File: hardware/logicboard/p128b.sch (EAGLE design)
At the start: 43 parts, among them IC1 74LS595N, IC10 74LS595N, IC11 74LS595N, IC12 74LS595N, IC13 74LS595N, IC14 74LS595N, IC15 74LS595N, IC16 74LS595N, IC2 74LS595N, IC3 74LS595N, IC4 74LS595N, IC5 74LS595N, IC6 74LS595N, IC7 74LS595N, IC8 74LS595N, IC9 74LS595N

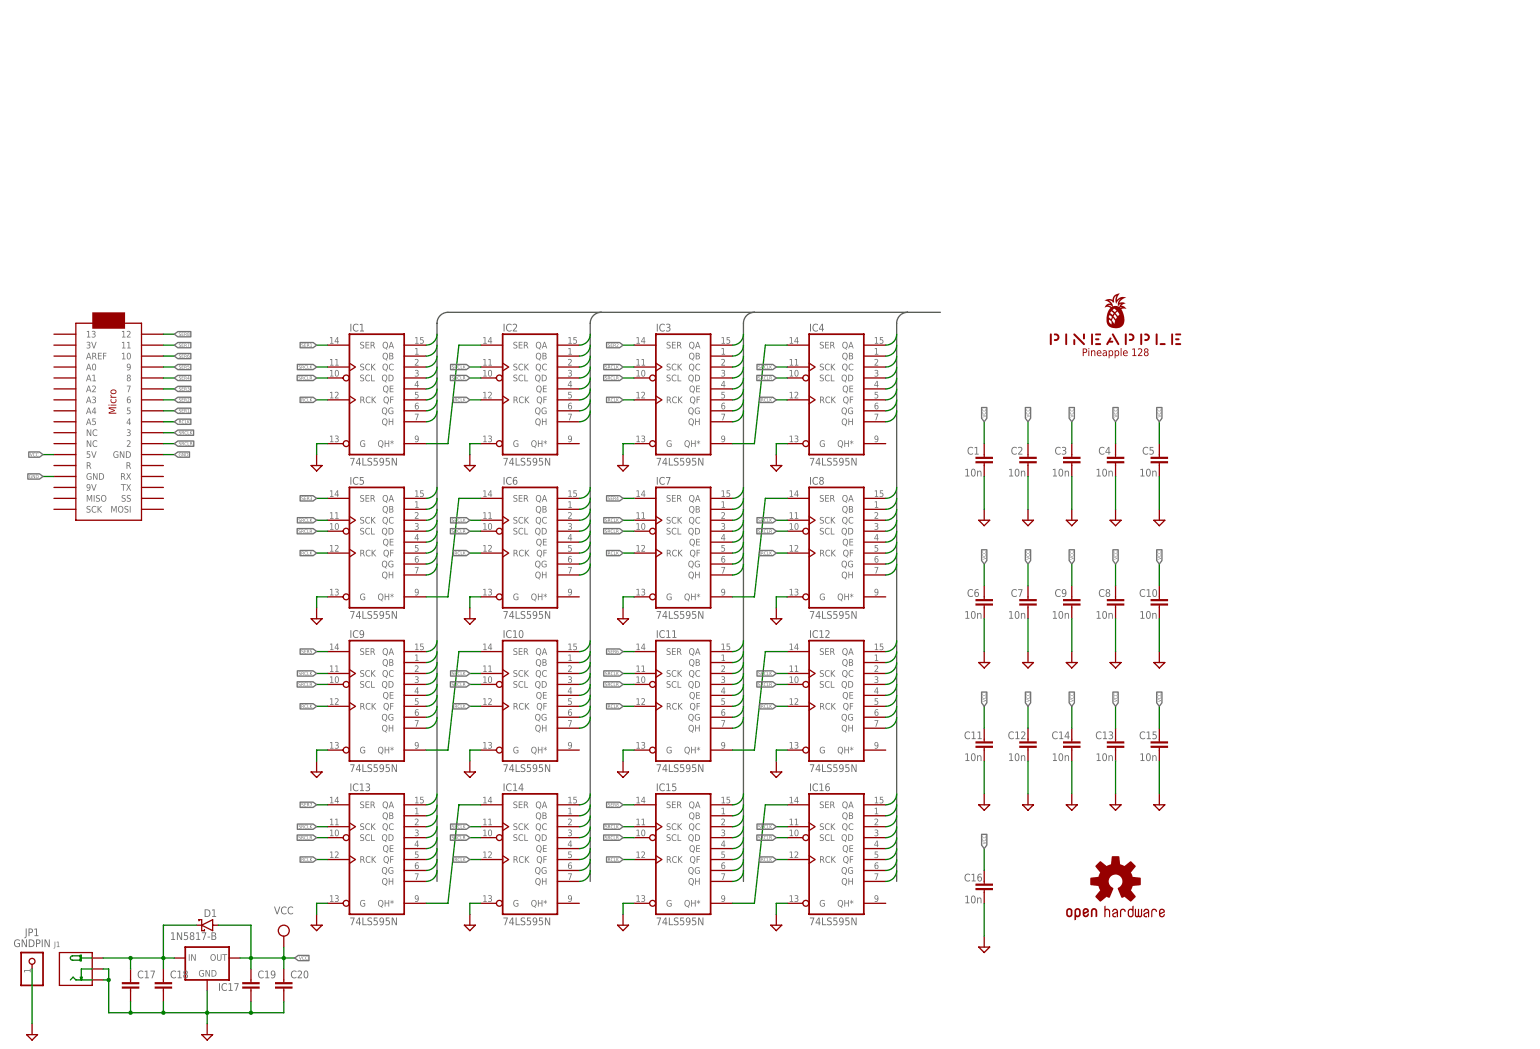
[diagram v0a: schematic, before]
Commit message: Separated into 2 boards.
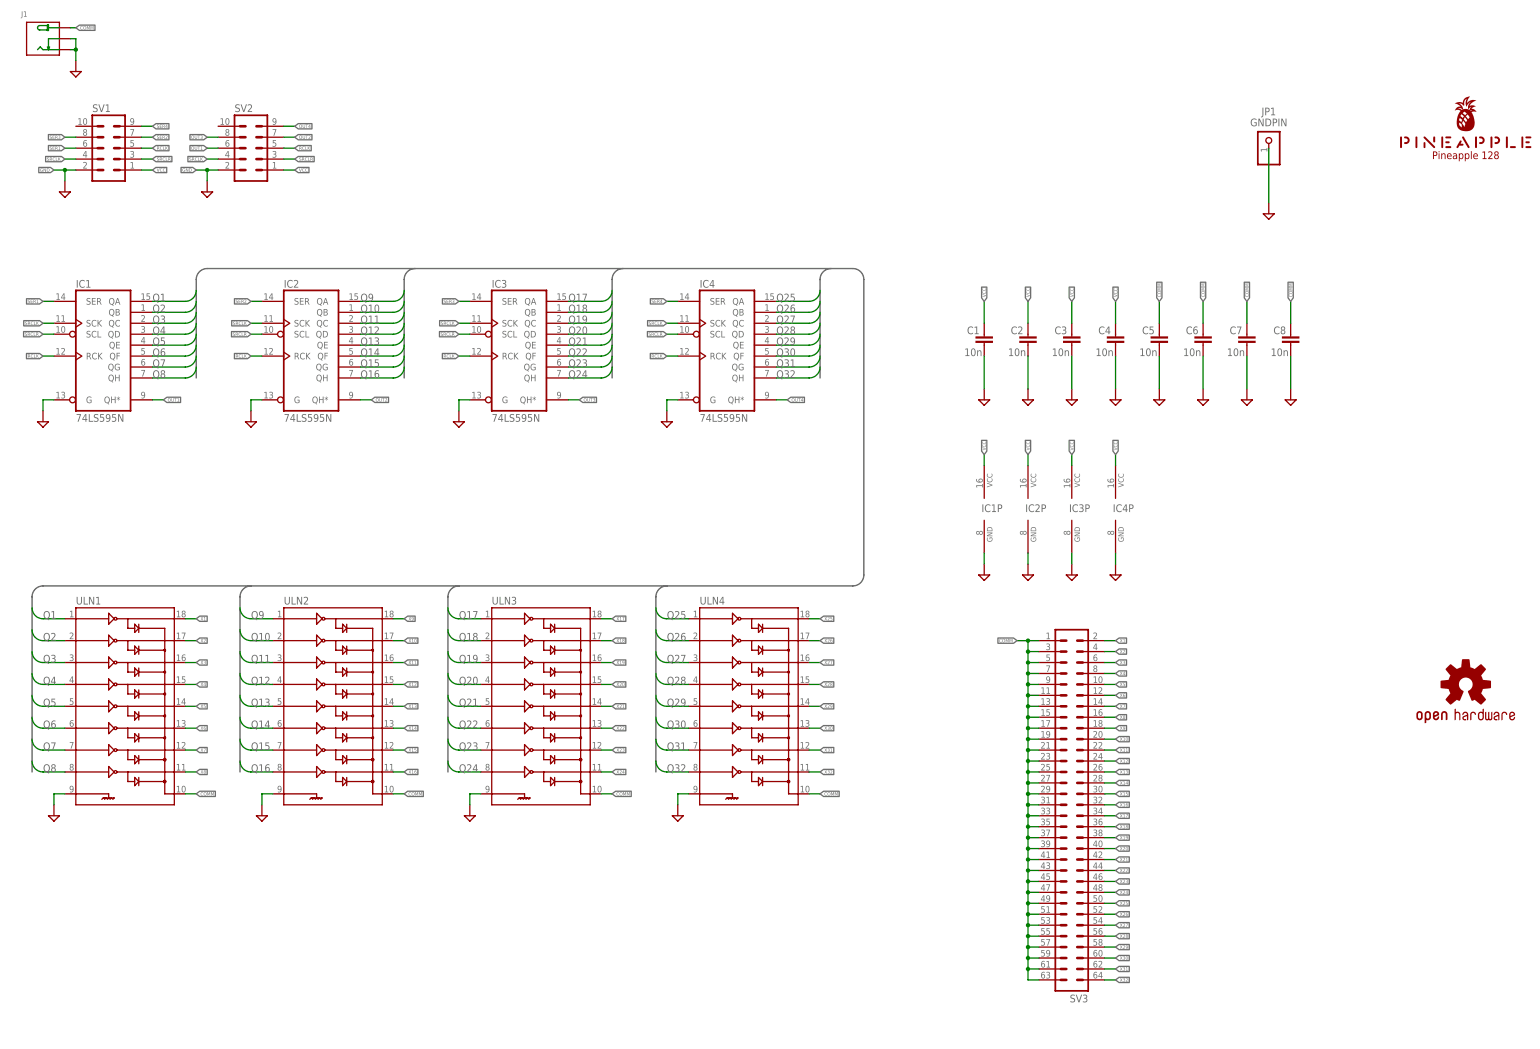
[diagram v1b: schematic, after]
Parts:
- removed C10, C15: 10n, rcl:C-EU025-024X044
- removed C11, C12, C13, C14, C16, C9: 10n, resistor:C-EU025-024X044
- removed C17: (no value), rcl:C-EU025-050X050
- removed C18, C19: (no value), rcl:C-EU050-024X044
- removed C20: (no value), rcl:C-EU025-024X044
- removed D1: 1N5817-B, diode:1N5817-B
- removed IC10, IC11, IC12, IC13, IC14, IC15, IC16, IC5, IC6, IC7, IC8, IC9: 74LS595N, 74xx-us:74LS595N
- removed IC17: (no value), v-reg:78MXXS
- removed MC1: ARDUINOMICRO, adafruit:ARDUINOMICRO
- added SV1, SV2: (no value), con-ml:ML10L
- added SV3: (no value), con-ml:ML64L
- added ULN1, ULN2, ULN3, ULN4: (no value), SparkFun-IC-Special-Function:ULN2803DIP
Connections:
- removed net N$1: IC1A.QH*, IC2A.SER
- removed net N$2: IC3A.QH*, IC4A.SER
- removed net N$3: IC5A.QH*, IC6A.SER
- removed net N$4: IC7A.QH*, IC8A.SER
- removed net N$5: IC10A.SER, IC9A.QH*
- removed net N$6: IC11A.QH*, IC12A.SER
- removed net N$7: IC13A.QH*, IC14A.SER
- removed net N$8: C17.1, C18.1, D1.C, IC17.IN, J1.+
- removed net N$9: IC15A.QH*, IC16A.SER
- removed net Q100: IC13A.QD
- removed net Q101: IC13A.QE
- removed net Q102: IC13A.QF
- removed net Q103: IC13A.QG
- removed net Q104: IC13A.QH
- removed net Q105: IC14A.QA
- removed net Q106: IC14A.QB
- removed net Q107: IC14A.QC
- removed net Q108: IC14A.QD
- removed net Q109: IC14A.QE
- removed net Q110: IC14A.QF
- removed net Q111: IC14A.QG
- removed net Q112: IC14A.QH
- removed net Q113: IC15A.QA
- removed net Q114: IC15A.QB
- removed net Q115: IC15A.QC
- removed net Q116: IC15A.QD
- removed net Q117: IC15A.QE
- removed net Q118: IC15A.QF
- removed net Q119: IC15A.QG
- removed net Q120: IC15A.QH
- removed net Q121: IC16A.QA
- removed net Q122: IC16A.QB
- removed net Q123: IC16A.QC
- removed net Q124: IC16A.QD
- removed net Q125: IC16A.QE
- removed net Q126: IC16A.QF
- removed net Q127: IC16A.QG
- removed net Q128: IC16A.QH
- removed net Q33: IC5A.QA
- removed net Q34: IC5A.QB
- removed net Q35: IC5A.QC
- removed net Q36: IC5A.QD
- removed net Q37: IC5A.QE
- removed net Q38: IC5A.QF
- removed net Q39: IC5A.QG
- removed net Q40: IC5A.QH
- removed net Q41: IC6A.QA
- removed net Q42: IC6A.QB
- removed net Q43: IC6A.QC
- removed net Q44: IC6A.QD
- removed net Q45: IC6A.QE
- removed net Q46: IC6A.QF
- removed net Q47: IC6A.QG
- removed net Q48: IC6A.QH
- removed net Q49: IC7A.QA
- removed net Q50: IC7A.QB
- removed net Q51: IC7A.QC
- removed net Q52: IC7A.QD
- removed net Q53: IC7A.QE
- removed net Q54: IC7A.QF
- removed net Q55: IC7A.QG
- removed net Q56: IC7A.QH
- removed net Q57: IC8A.QA
- removed net Q58: IC8A.QB
- removed net Q59: IC8A.QC
- removed net Q60: IC8A.QD
- removed net Q61: IC8A.QE
- removed net Q62: IC8A.QF
- removed net Q63: IC8A.QG
- removed net Q64: IC8A.QH
- removed net Q65: IC9A.QA
- removed net Q66: IC9A.QB
- removed net Q67: IC9A.QC
- removed net Q68: IC9A.QD
- removed net Q69: IC9A.QE
- removed net Q70: IC9A.QF
- removed net Q71: IC9A.QG
- removed net Q72: IC9A.QH
- removed net Q73: IC10A.QA
- removed net Q74: IC10A.QB
- removed net Q75: IC10A.QC
- removed net Q76: IC10A.QD
- removed net Q77: IC10A.QE
- removed net Q78: IC10A.QF
- removed net Q79: IC10A.QG
- removed net Q80: IC10A.QH
- removed net Q81: IC11A.QA
- removed net Q82: IC11A.QB
- removed net Q83: IC11A.QC
- removed net Q84: IC11A.QD
- removed net Q85: IC11A.QE
- removed net Q86: IC11A.QF
- removed net Q87: IC11A.QG
- removed net Q88: IC11A.QH
- removed net Q89: IC12A.QA
- removed net Q90: IC12A.QB
- removed net Q91: IC12A.QC
- removed net Q92: IC12A.QD
- removed net Q93: IC12A.QE
- removed net Q94: IC12A.QF
- removed net Q95: IC12A.QG
- removed net Q96: IC12A.QH
- removed net Q97: IC13A.QA
- removed net Q98: IC13A.QB
- removed net Q99: IC13A.QC
- removed net SER5: IC9A.SER, MC1.9
- removed net SER6: IC11A.SER, MC1.10
- removed net SER7: IC13A.SER, MC1.11
- removed net SER8: IC15A.SER, MC1.12
- new net COMM: C5.1, C6.1, C7.1, C8.1, J1.+, SV3.1, SV3.11, SV3.13, SV3.15, SV3.17, SV3.19, SV3.21, SV3.23, SV3.25, SV3.27, SV3.29, SV3.3, SV3.31, SV3.33, SV3.35, SV3.37, SV3.39, SV3.41, SV3.43, SV3.45, SV3.47, SV3.49, SV3.5, SV3.51, SV3.53, SV3.55, SV3.57, SV3.59, SV3.61, SV3.63, SV3.7, SV3.9, ULN1.10, ULN2.10, ULN3.10, ULN4.10
- new net OUT1: IC1A.QH*, SV2.6
- new net OUT2: IC2A.QH*, SV2.7
- new net OUT3: IC3A.QH*, SV2.8
- new net OUT4: IC4A.QH*, SV2.9
- new net X1: SV3.2, ULN1.18
- new net X10: SV3.20, ULN2.17
- new net X11: SV3.22, ULN2.16
- new net X12: SV3.24, ULN2.15
- new net X13: SV3.26, ULN2.14
- new net X14: SV3.28, ULN2.13
- new net X15: SV3.30, ULN2.12
- new net X16: SV3.32, ULN2.11
- new net X17: SV3.34, ULN3.18
- new net X18: SV3.36, ULN3.17
- new net X19: SV3.38, ULN3.16
- new net X2: SV3.4, ULN1.17
- new net X20: SV3.40, ULN3.15
- new net X21: SV3.42, ULN3.14
- new net X22: SV3.44, ULN3.13
- new net X23: SV3.46, ULN3.12
- new net X24: SV3.48, ULN3.11
- new net X25: SV3.50, ULN4.18
- new net X26: SV3.52, ULN4.17
- new net X27: SV3.54, ULN4.16
- new net X28: SV3.56, ULN4.15
- new net X29: SV3.58, ULN4.14
- new net X3: SV3.6, ULN1.16
- new net X30: SV3.60, ULN4.13
- new net X31: SV3.62, ULN4.12
- new net X32: SV3.64, ULN4.11
- new net X4: SV3.8, ULN1.15
- new net X5: SV3.10, ULN1.14
- new net X6: SV3.12, ULN1.13
- new net X7: SV3.14, ULN1.12
- new net X8: SV3.16, ULN1.11
- new net X9: SV3.18, ULN2.18
- net GND: now also IC1P.GND, IC2P.GND, IC3P.GND, IC4P.GND, SV1.2, SV2.2, ULN1.9, ULN2.9, ULN3.9, ULN4.9; no longer C10.2, C11.2, C12.2, C13.2, C14.2, C15.2, C16.2, C17.2, C18.2, C19.2, C20.2, C9.2, IC10A.G, IC11A.G, IC12A.G, IC13A.G, IC14A.G, IC15A.G, IC16A.G, IC17.GND, IC5A.G, IC6A.G, IC7A.G, IC8A.G, IC9A.G, MC1.GND, MC1.GND@1
- net Q1: now also ULN1.1
- net Q10: now also ULN2.2
- net Q11: now also ULN2.3
- net Q12: now also ULN2.4
- net Q13: now also ULN2.5
- net Q14: now also ULN2.6
- net Q15: now also ULN2.7
- net Q16: now also ULN2.8
- net Q17: now also ULN3.1
- net Q18: now also ULN3.2
- net Q19: now also ULN3.3
- net Q2: now also ULN1.2
- net Q20: now also ULN3.4
- net Q21: now also ULN3.5
- net Q22: now also ULN3.6
- net Q23: now also ULN3.7
- net Q24: now also ULN3.8
- net Q25: now also ULN4.1
- net Q26: now also ULN4.2
- net Q27: now also ULN4.3
- net Q28: now also ULN4.4
- net Q29: now also ULN4.5
- net Q3: now also ULN1.3
- net Q30: now also ULN4.6
- net Q31: now also ULN4.7
- net Q32: now also ULN4.8
- net Q4: now also ULN1.4
- net Q5: now also ULN1.5
- net Q6: now also ULN1.6
- net Q7: now also ULN1.7
- net Q8: now also ULN1.8
- net Q9: now also ULN2.1
- net RCLK: now also SV1.5, SV2.5; no longer IC10A.RCK, IC11A.RCK, IC12A.RCK, IC13A.RCK, IC14A.RCK, IC15A.RCK, IC16A.RCK, IC5A.RCK, IC6A.RCK, IC7A.RCK, IC8A.RCK, IC9A.RCK, MC1.4
- net SER1: now also SV1.6; no longer MC1.5
- net SER2: now also IC2A.SER, SV1.7; no longer IC3A.SER, MC1.6
- net SER3: now also IC3A.SER, SV1.8; no longer IC5A.SER, MC1.7
- net SER4: now also IC4A.SER, SV1.9; no longer IC7A.SER, MC1.8
- net SRCLK: now also SV1.4, SV2.4; no longer IC10A.SCK, IC11A.SCK, IC12A.SCK, IC13A.SCK, IC14A.SCK, IC15A.SCK, IC16A.SCK, IC5A.SCK, IC6A.SCK, IC7A.SCK, IC8A.SCK, IC9A.SCK, MC1.3
- net SRCLR: now also SV1.3, SV2.3; no longer IC10A.SCL, IC11A.SCL, IC12A.SCL, IC13A.SCL, IC14A.SCL, IC15A.SCL, IC16A.SCL, IC5A.SCL, IC6A.SCL, IC7A.SCL, IC8A.SCL, IC9A.SCL, MC1.2
- net VCC: now also IC1P.VCC, IC2P.VCC, IC3P.VCC, IC4P.VCC, SV1.1, SV2.1; no longer C10.1, C11.1, C12.1, C13.1, C14.1, C15.1, C16.1, C19.1, C20.1, C5.1, C6.1, C7.1, C8.1, C9.1, D1.A, IC17.OUT, MC1.5V
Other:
- moved on the sheet: C1, C2, C3, C4, C5, C6, C7, C8, IC1, IC2, IC3, IC4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
